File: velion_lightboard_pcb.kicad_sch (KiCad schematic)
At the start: 133 parts, among them J1 Conn_01x04, J10 Conn_01x03, J11 Conn_01x04, J12 Conn_01x04, J13 Conn_01x03, J14 Conn_01x03, J15 Conn_01x03, J16 Conn_01x03, J17 Conn_01x04, J2 Conn_01x04, J3 Conn_01x03, J4 Conn_01x04, J5 Conn_01x04, J6 Conn_01x04, J7 Conn_01x03, J8 Conn_01x03, J9 Conn_01x03, Q0 NMOS, Q1 BSS123-7-F, Q10 BSS123-7-F, Q11 NMOS, Q12 NMOS, Q13 BSS123-7-F, Q14 BSS123-7-F, Q15 BSS123-7-F, Q16 BSS123-7-F, Q17 NMOS, Q18 NMOS, Q19 NMOS, Q2 BSS123-7-F, Q3 BSS123-7-F, Q4 BSS123-7-F, Q5 NMOS, Q6 NMOS, Q7 BSS123-7-F, Q8 BSS123-7-F, Q9 BSS123-7-F, U1 ESP32-C3_SUPERMINI_TH, U10 MCP6L01x-xOT, U11 LM2104DR, U12 LM2104DR, U13 LM2104DR, U14 ADS1115IDGS, U2 MCP23017_SO, U3 LM2104DR, U4 LM2104DR, U5 MCP6L01x-xOT, U6 ADS1115IDGS, U7 MCP6L01x-xOT, U8 TJA1051T-3, U9 LM2104DR

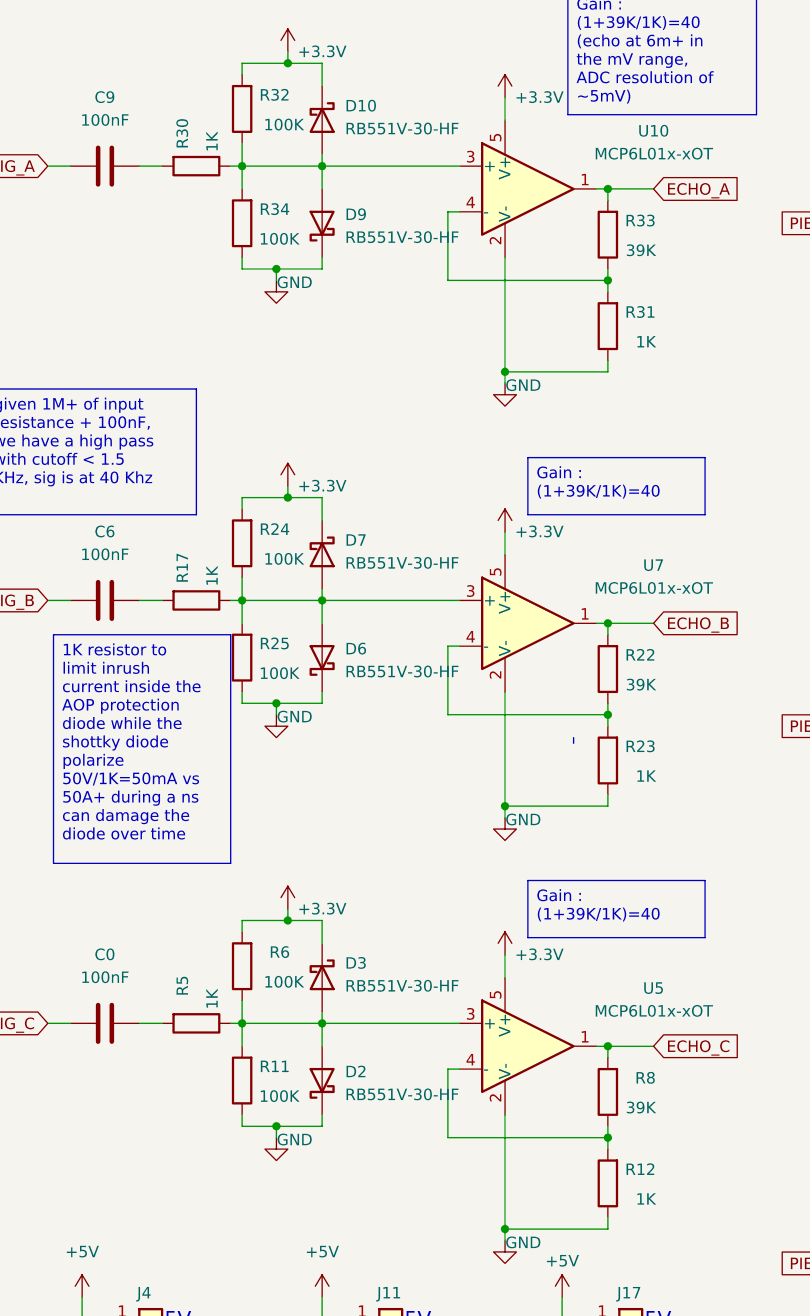
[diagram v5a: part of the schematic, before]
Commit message: generated fab file, added capacitor for low pass/antialiasing in  Sonar
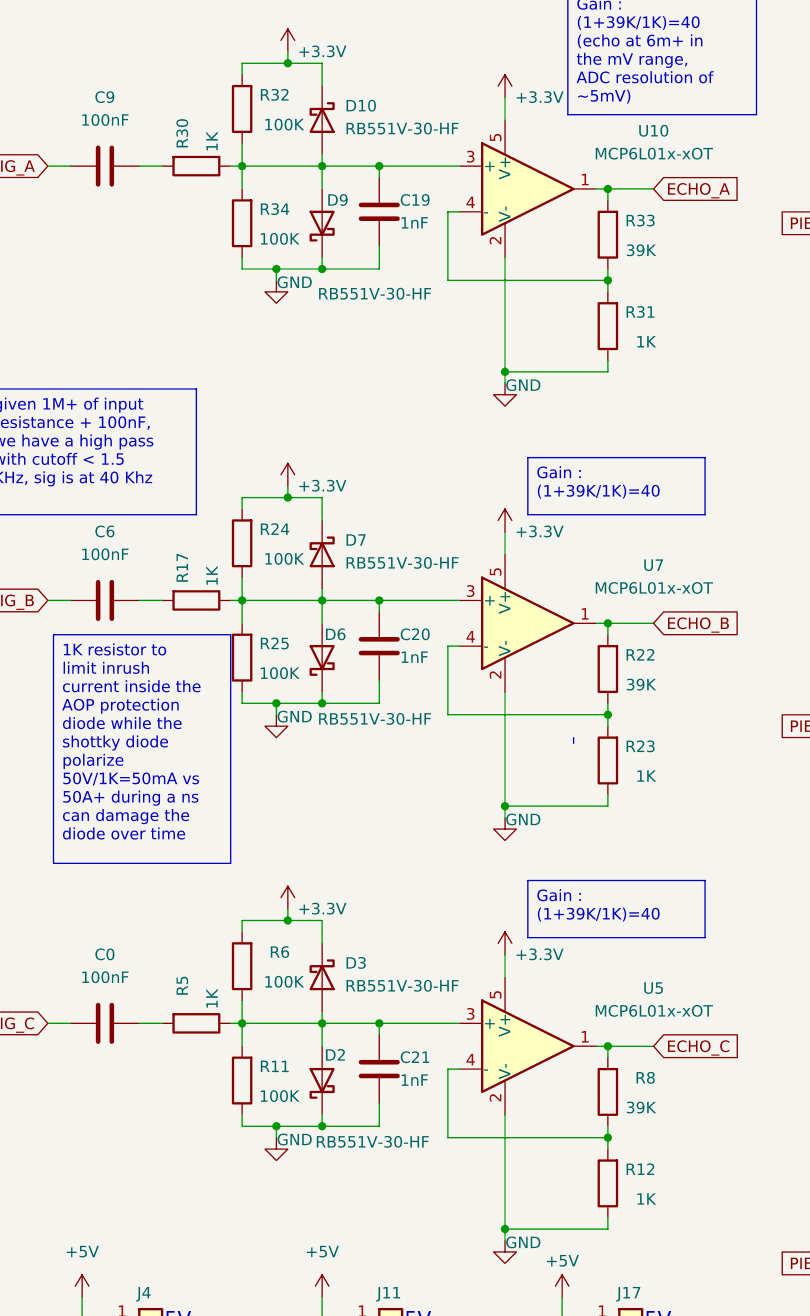
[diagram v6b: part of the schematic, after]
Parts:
- added C19, C20, C21: 1nF, Capacitor_SMD:C_1206_3216Metric_Pad1.33x1.80mm_HandSolder, symbol Device:C
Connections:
- net GND: now also C19.1, C20.1, C21.1
- net at D2.2 (A), D3.2 (A), R11.2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: now also C21.2
- net at D6.2 (A), D7.2 (A), R17.1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: now also C20.2
- net at D10.2 (A), D9.2 (A), R30.1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: now also C19.2

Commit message: replaced the light sensor pin header by a standard bornier
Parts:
- J12: footprint Connector_PinHeader_2.54mm:PinHeader_1x04_P2.54mm_Vertical -> velion_mainboard:15EDG-4P
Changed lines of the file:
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@@
 			)
 		)
-		(property "Footprint" "Connector_PinHeader_2.54mm:PinHeader_1x04_P2.54mm_Vertical"
+		(property "Footprint" "velion_mainboard:15EDG-4P"
 			(at 163.83 271.78 0)
 			(effects

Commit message: adding BOM for mouser
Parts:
- U14, U6: footprint Package_SO:TSSOP-10_3x3mm_P0.5mm -> Package_SO:VSSOP-10_3x3mm_P0.5mm
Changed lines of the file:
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@@
 			)
 		)
-		(property "Footprint" "Package_SO:TSSOP-10_3x3mm_P0.5mm"
+		(property "Footprint" "Package_SO:VSSOP-10_3x3mm_P0.5mm"
 			(at 45.72 194.31 0)
 			(effects
@@
 			)
 		)
-		(property "Footprint" "Package_SO:TSSOP-10_3x3mm_P0.5mm"
+		(property "Footprint" "Package_SO:VSSOP-10_3x3mm_P0.5mm"
 			(at 97.79 194.31 0)
 			(effects
